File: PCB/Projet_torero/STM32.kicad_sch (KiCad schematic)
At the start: 24 parts, among them J1 Conn_02x07_Odd_Even, J3 Conn_01x09, SW1 SW_Push, SW2 SW_Push, U1 STM32G431CBUx, Y1 Crystal_GND24_Small

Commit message: modif capteur
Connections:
- net ANALOG_OUTPUT_1 renamed ANALOG_OUTPUT_CAPT_BORD_1
- net ANALOG_OUTPUT_2 renamed ANALOG_OUTPUT_CAPT_BORD_2
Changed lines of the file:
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@@
 		)
 	)
-	(hierarchical_label "ANALOG_OUTPUT_2"
+	(hierarchical_label "ANALOG_OUTPUT_CAPT_BORD_2"
 		(shape input)
 		(at 77.47 111.76 180)
@@
 		)
 	)
-	(hierarchical_label "ANALOG_OUTPUT_1"
+	(hierarchical_label "ANALOG_OUTPUT_CAPT_BORD_1"
 		(shape input)
 		(at 77.47 109.22 180)

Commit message: review sch
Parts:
- C3: value 0.1 p -> 0p1
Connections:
- net ANALOG_OUTPUT_CAPT_BORD_1 renamed ANALOG_OUTPUT_CAPT_BORD_G
- net ANALOG_OUTPUT_CAPT_BORD_2 renamed ANALOG_OUTPUT_CAPT_BORD_D
- net CS renamed CS_ACC
- net DEV_EN renamed DEV_EN_LIDAR
- net INT1 renamed INT1_ACC
- net INT2 renamed INT2_ACC
- net M_EN renamed M_EN_LIDAR
- net M_SCTR renamed M_SCTR_LIDAR
- net Rx renamed Rx_LIDAR
- net SCLK renamed SCLK_ACC
- net SDA/SDI/SDIO renamed SDI_ACC
- net SDO/ADDR renamed SDO_ACC
- net Tx renamed Tx_LIDAR
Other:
- note added: "Roue de LED pour debogg Lidar"
- moved on the sheet: J3
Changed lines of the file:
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@@
 	(wire
 		(pts
-			(xy 205.74 128.27) (xy 208.28 128.27)
+			(xy 226.06 139.7) (xy 228.6 139.7)
 		)
 		(stroke
@@
 	(wire
 		(pts
-			(xy 78.74 48.26) (xy 90.17 48.26)
-		)
-		(stroke
-			(width 0)
-			(type default)
-		)
-	)
-	(wire
-		(pts
 			(xy 60.96 64.77) (xy 57.15 64.77)
 		)
@@
 	(wire
 		(pts
-			(xy 205.74 132.08) (xy 205.74 128.27)
+			(xy 226.06 143.51) (xy 226.06 139.7)
 		)
 		(stroke
@@
 		)
 	)
+	(text "Roue de LED pour debogg Lidar\n"
+		(exclude_from_sim no)
+		(at 232.156 115.062 0)
+		(effects
+			(font
+				(size 1.27 1.27)
+			)
+		)
+	)
 	(global_label "VCP_RX"
 		(shape input)
@@
 	(global_label "LED_N"
 		(shape input)
-		(at 208.28 107.95 180)
+		(at 228.6 119.38 180)
 		(fields_autoplaced yes)
 		(effects
@@
 		)
 		(property "Intersheetrefs" "${INTERSHEET_REFS}"
-			(at 199.5496 107.95 0)
+			(at 219.8696 119.38 0)
 			(effects
 				(font
@@
 	(global_label "LED_SW"
 		(shape input)
-		(at 208.28 125.73 180)
+		(at 228.6 137.16 180)
 		(fields_autoplaced yes)
 		(effects
@@
 		)
 		(property "Intersheetrefs" "${INTERSHEET_REFS}"
-			(at 198.2192 125.73 0)
+			(at 218.5392 137.16 0)
 			(effects
 				(font
@@
 	(global_label "LED_SE"
 		(shape input)
-		(at 208.28 123.19 180)
+		(at 228.6 134.62 180)
 		(fields_autoplaced yes)
 		(effects
@@
 		)
 		(property "Intersheetrefs" "${INTERSHEET_REFS}"
-			(at 198.5216 123.19 0)
+			(at 218.8416 134.62 0)
 			(effects
 				(font
@@
 	(global_label "LED_NE"
 		(shape input)
-		(at 208.28 118.11 180)
+		(at 228.6 129.54 180)
 		(fields_autoplaced yes)
 		(effects
@@
 		)
 		(property "Intersheetrefs" "${INTERSHEET_REFS}"
-			(at 198.4006 118.11 0)
+			(at 218.7206 129.54 0)
 			(effects
 				(font
@@
 	(global_label "LED_W"
 		(shape input)
-		(at 208.28 115.57 180)
+		(at 228.6 127 180)
 		(fields_autoplaced yes)
 		(effects
@@
 		)
 		(property "Intersheetrefs" "${INTERSHEET_REFS}"
-			(at 199.4287 115.57 0)
+			(at 219.7487 127 0)
 			(effects
 				(font
@@
 	(global_label "LED_S"
 		(shape input)
-		(at 208.28 113.03 180)
+		(at 228.6 124.46 180)
 		(fields_autoplaced yes)
 		(effects
@@
 		)
 		(property "Intersheetrefs" "${INTERSHEET_REFS}"
-			(at 199.6706 113.03 0)
+			(at 219.9906 124.46 0)
 			(effects
 				(font
@@
 	(global_label "LED_NW"
 		(shape input)
-		(at 208.28 120.65 180)
+		(at 228.6 132.08 180)
 		(fields_autoplaced yes)
 		(effects
@@
 		)
 		(property "Intersheetrefs" "${INTERSHEET_REFS}"
-			(at 198.0982 120.65 0)
+			(at 218.4182 132.08 0)
 			(effects
 				(font
@@
 	(global_label "LED_E"
 		(shape input)
-		(at 208.28 110.49 180)
+		(at 228.6 121.92 180)
 		(fields_autoplaced yes)
 		(effects
@@
 		)
 		(property "Intersheetrefs" "${INTERSHEET_REFS}"
-			(at 199.7311 110.49 0)
+			(at 220.0511 121.92 0)
 			(effects
 				(font
@@
 		)
 	)
-	(hierarchical_label "INT1"
+	(hierarchical_label "INT1_ACC"
 		(shape input)
 		(at 110.49 96.52 0)
@@
 		)
 	)
-	(hierarchical_label "M_EN"
+	(hierarchical_label "M_EN_LIDAR"
 		(shape input)
 		(at 77.47 114.3 180)
@@
 		)
 	)
-	(hierarchical_label "INT2"
+	(hierarchical_label "INT2_ACC"
 		(shape input)
 		(at 77.47 99.06 180)
@@
 		)
 	)
-	(hierarchical_label "SCLK"
+	(hierarchical_label "SCLK_ACC"
 		(shape input)
 		(at 77.47 83.82 180)
@@
 		)
 	)
-	(hierarchical_label "Tx"
+	(hierarchical_label "Tx_LIDAR"
 		(shape input)
 		(at 77.47 137.16 180)
@@
 		)
 	)
-	(hierarchical_label "CS"
+	(hierarchical_label "CS_ACC"
 		(shape input)
 		(at 110.49 83.82 0)
@@
 		)
 	)
-	(hierarchical_label "ANALOG_OUTPUT_CAPT_BORD_2"
+	(hierarchical_label "ANALOG_OUTPUT_CAPT_BORD_D"
 		(shape input)
 		(at 77.47 111.76 180)
@@
 		)
 	)
-	(hierarchical_label "SDA{slash}SDI{slash}SDIO"
+	(hierarchical_label "SDI_ACC"
 		(shape input)
 		(at 77.47 147.32 180)
@@
 		)
 	)
-	(hierarchical_label "Rx"
+	(hierarchical_label "Rx_LIDAR"
 		(shape input)
 		(at 77.47 134.62 180)
@@
 		)
 	)
-	(hierarchical_label "SDO{slash}ADDR"
+	(hierarchical_label "SDO_ACC"
 		(shape input)
 		(at 77.47 144.78 180)
@@
 		)
 	)
-	(hierarchical_label "ANALOG_OUTPUT_CAPT_BORD_1"
+	(hierarchical_label "ANALOG_OUTPUT_CAPT_BORD_G"
 		(shape input)
 		(at 77.47 109.22 180)
@@
 		)
 	)
-	(hierarchical_label "DEV_EN"
+	(hierarchical_label "DEV_EN_LIDAR"
 		(shape input)
 		(at 77.47 116.84 180)
@@
 		)
 	)
-	(hierarchical_label "M_SCTR"
+	(hierarchical_label "M_SCTR_LIDAR"
 		(shape input)
 		(at 77.47 119.38 180)
@@
 	(symbol
 		(lib_id "power:GND")
-		(at 205.74 132.08 0)
+		(at 226.06 143.51 0)
 		(unit 1)
 		(exclude_from_sim no)
@@
 		(fields_autoplaced yes)
 		(property "Reference" "#PWR029"
-			(at 205.74 138.43 0)
+			(at 226.06 149.86 0)
 			(effects
 				(font
@@
 		)
 		(property "Value" "GND"
-			(at 205.74 137.16 0)
+			(at 226.06 148.59 0)
 			(effects
 				(font
@@
 		)
 		(property "Footprint" ""
-			(at 205.74 132.08 0)
+			(at 226.06 143.51 0)
 			(effects
 				(font
@@
 		)
 		(property "Datasheet" ""
-			(at 205.74 132.08 0)
+			(at 226.06 143.51 0)
 			(effects
 				(font
@@
 		)
 		(property "Description" "Power symbol creates a global label with name \"GND\" , ground"
-			(at 205.74 132.08 0)
+			(at 226.06 143.51 0)
 			(effects
 				(font
@@
 	(symbol
 		(lib_id "Connector_Generic:Conn_01x09")
-		(at 213.36 118.11 0)
+		(at 233.68 129.54 0)
 		(unit 1)
 		(exclude_from_sim no)
@@
 		(fields_autoplaced yes)
 		(property "Reference" "J3"
-			(at 215.9 116.8399 0)
+			(at 236.22 128.2699 0)
 			(effects
 				(font
@@
 		)
 		(property "Value" "Conn_01x09"
-			(at 215.9 119.3799 0)
+			(at 236.22 130.8099 0)
 			(effects
 				(font
@@
 		)
 		(property "Footprint" ""
-			(at 213.36 118.11 0)
+			(at 233.68 129.54 0)
 			(effects
 				(font
@@
 		)
 		(property "Datasheet" "~"
-			(at 213.36 118.11 0)
+			(at 233.68 129.54 0)
 			(effects
 				(font
@@
 		)
 		(property "Description" "Generic connector, single row, 01x09, script generated (kicad-library-utils/schlib/autogen/connector/)"
-			(at 213.36 118.11 0)
+			(at 233.68 129.54 0)
 			(effects
 				(font
@@
 			)
 		)
-		(property "Value" "0.1 p"
+		(property "Value" "0p1"
 			(at 56.134 82.804 0)
 			(effects
@@
 	(symbol
 		(lib_id "power:+3.3V")
-		(at 78.74 48.26 90)
+		(at 90.17 48.26 0)
 		(unit 1)
 		(exclude_from_sim no)
@@
 		(on_board yes)
 		(dnp no)
-		(fields_autoplaced yes)
 		(property "Reference" "#PWR04"
-			(at 82.55 48.26 0)
+			(at 90.17 52.07 0)
 			(effects
 				(font
@@
 		)
 		(property "Value" "+3.3V"
-			(at 74.93 48.2599 90)
+			(at 86.868 43.942 0)
 			(effects
 				(font
@@
 		)
 		(property "Footprint" ""
-			(at 78.74 48.26 0)
+			(at 90.17 48.26 0)
 			(effects
 				(font
@@
 		)
 		(property "Datasheet" ""
-			(at 78.74 48.26 0)
+			(at 90.17 48.26 0)
 			(effects
 				(font
@@
 		)
 		(property "Description" "Power symbol creates a global label with name \"+3.3V\""
-			(at 78.74 48.26 0)
+			(at 90.17 48.26 0)
 			(effects
 				(font

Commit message: review sch 2
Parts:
- 10k: value R_Small -> 10k
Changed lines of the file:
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@@
 			)
 		)
-		(property "Value" "R_Small"
+		(property "Value" "10k"
 			(at 26.416 132.08 90)
 			(effects

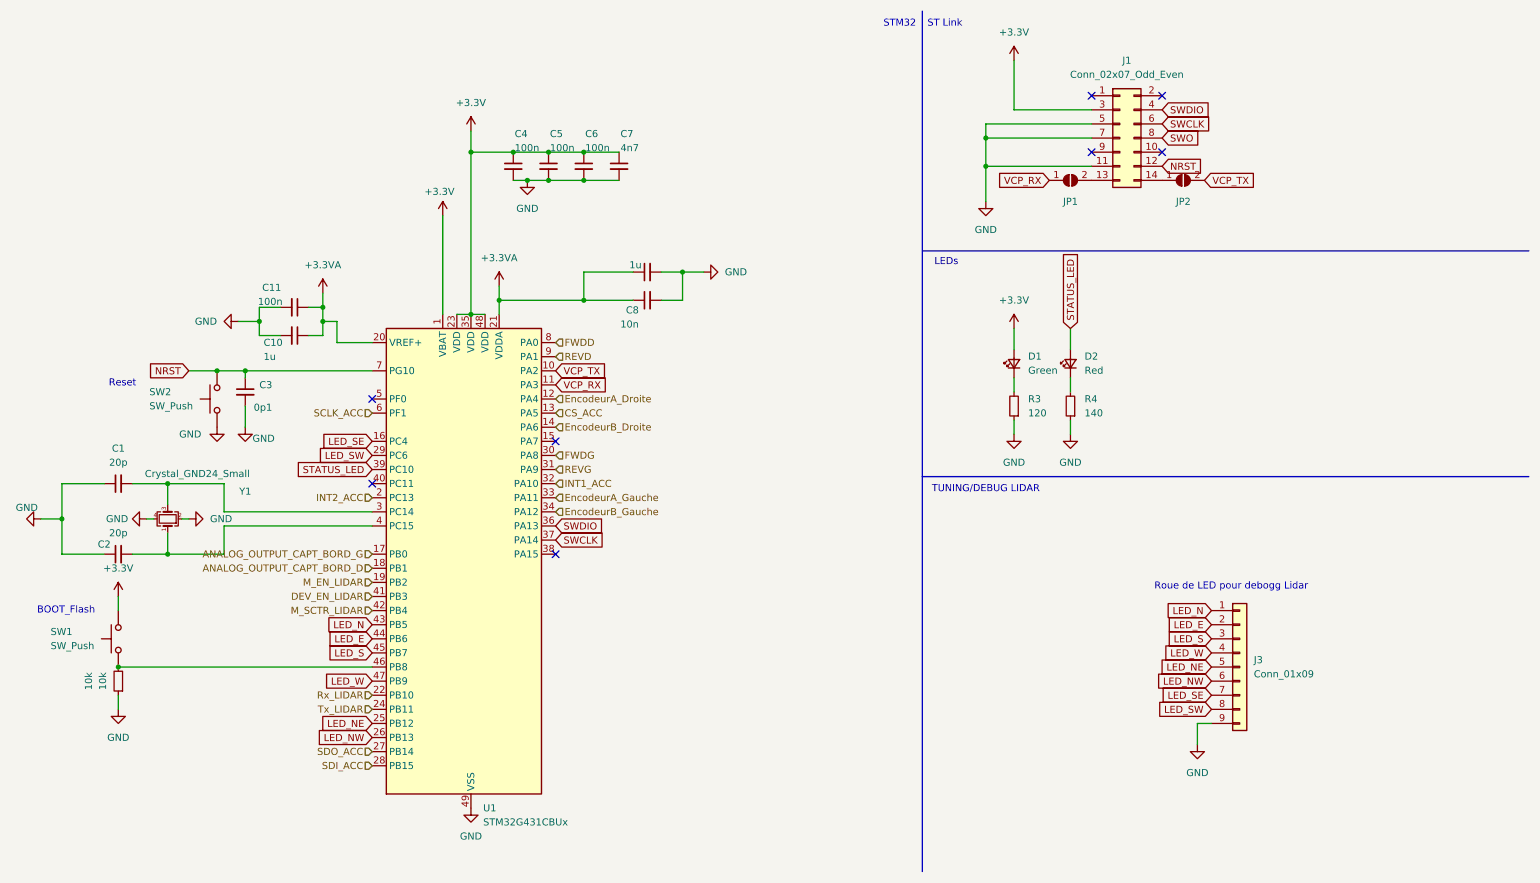
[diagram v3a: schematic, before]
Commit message: review sch après vérif prof
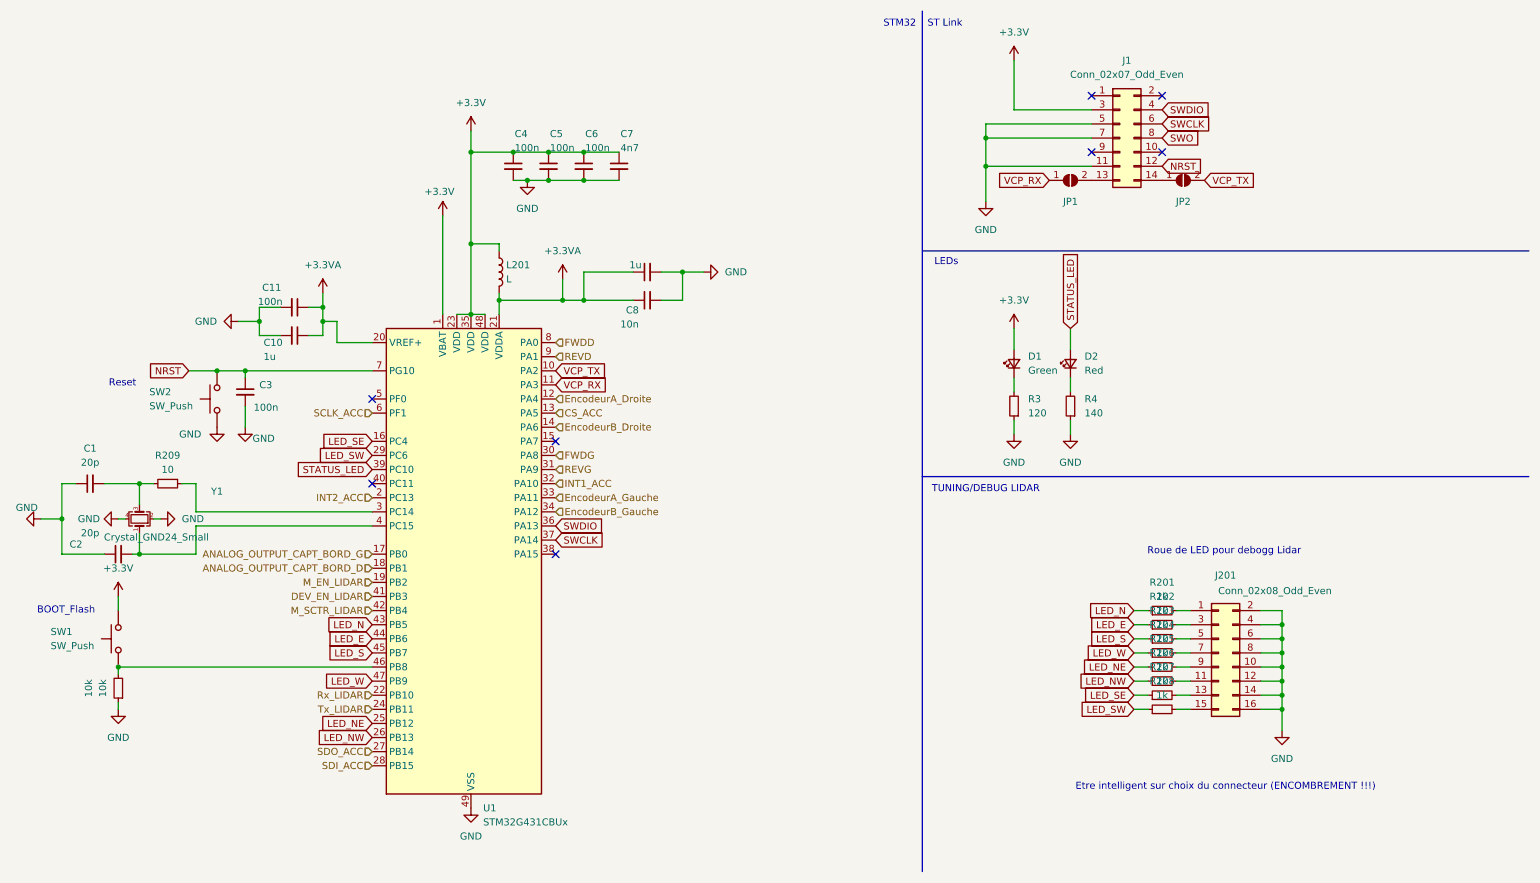
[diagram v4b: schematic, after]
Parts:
- removed J3: Conn_01x09, symbol Connector_Generic:Conn_01x09
- added J201: Conn_02x08_Odd_Even, symbol Connector_Generic:Conn_02x08_Odd_Even
- added L201: L, symbol Device:L
- added R201, R202, R203, R204, R205, R206, R207, R208: 1k, symbol Device:R_Small
- added R209: 10, Resistor_SMD:R_0603_1608Metric_Pad0.98x0.95mm_HandSolder, symbol Device:R_Small
- C3: value 0p1 -> 100n
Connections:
- net +3.3V: now also L201.1
- net +3.3VA: now also L201.2
- net GND: now also J201.10 (Pin_10), J201.12 (Pin_12), J201.14 (Pin_14), J201.16 (Pin_16), J201.2 (Pin_2), J201.4 (Pin_4), J201.6 (Pin_6), J201.8 (Pin_8)
- net LED_E: now also R202.1
- net LED_N: now also R201.1
- net LED_NE: now also R205.1
- net LED_NW: now also R206.1
- net LED_S: now also R203.1
- net LED_SE: now also R207.1
- net LED_SW: now also R208.1
- net LED_W: now also R204.1
- net at C1.2, Y1.3: now also R209.2; no longer U1.3 (PC14)
- new net: J201.15 (Pin_15), R208.2
- new net: J201.11 (Pin_11), R206.2
- new net: J201.3 (Pin_3), R202.2
- new net: R209.1, U1.3 (PC14)
- new net: J201.1 (Pin_1), R201.2
- new net: J201.13 (Pin_13), R207.2
- new net: J201.5 (Pin_5), R203.2
- new net: J201.7 (Pin_7), R204.2
- new net: J201.9 (Pin_9), R205.2
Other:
- note added: "Etre intelligent sur choix du connecteur (ENCOMBREMENT !!!)"
- moved on the sheet: 10k, C1, Y1
